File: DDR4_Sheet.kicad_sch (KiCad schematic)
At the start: 9 parts, among them U17002 Samsung K4A4G165WE-BCRC

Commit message: move DDR power decoupling capacitors into DDR4 Sheet
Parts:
- added C? (x6): 100nF X5R 10V, Capacitor_SMD:C_0402_1005Metric, symbol Device:C
- added C? (x10): 100nF X5R 6.3V, Capacitor_SMD:C_0201_0603Metric, symbol Device:C
- added C?: 1nF X5R 50V, Capacitor_SMD:C_0402_1005Metric, symbol Device:C
- added C?: 4.7uF X5R 10V, Capacitor_SMD:C_0402_1005Metric, symbol Device:C
- added C?: 22uF X5R 6.3V, Capacitor_SMD:C_0603_1608Metric, symbol Device:C
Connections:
- net V_{DD} is gone; now on net VCC1V2_DDR: U17002.B3 (V_{DD}), U17002.B9 (V_{DD}), U17002.D1 (V_{DD}), U17002.G7 (V_{DD}), U17002.J1 (V_{DD}), U17002.J9 (V_{DD}), U17002.L1 (V_{DD}), U17002.L9 (V_{DD}), U17002.R1 (V_{DD}), U17002.T9 (V_{DD})
- net V_{DDQ} renamed VCC1V2_DDR
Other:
- moved on the sheet: C?, R17002, R?, U17002B, U?A

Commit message: changed Power Label and copy DDR4 Sheets
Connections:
- net VCC1V2_DDR renamed VCC1V2

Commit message: connect new decoupling capacitors
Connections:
- net GND: now also C?.1, C?.1, C?.1, C?.1, C?.1, C?.1, C?.1, C?.1, C?.1, C?.1, C?.1, C?.1, C?.1, C?.1, C?.1, C?.1, C?.1, C?.1, C?.2
- net VCC1V2: now also C?.2, C?.2, C?.2, C?.2, C?.2, C?.2, C?.2, C?.2, C?.2, C?.2, C?.2, C?.2, C?.2, C?.2, C?.2
- net VCC2V5: now also C?.1, C?.2, C?.2, C?.2

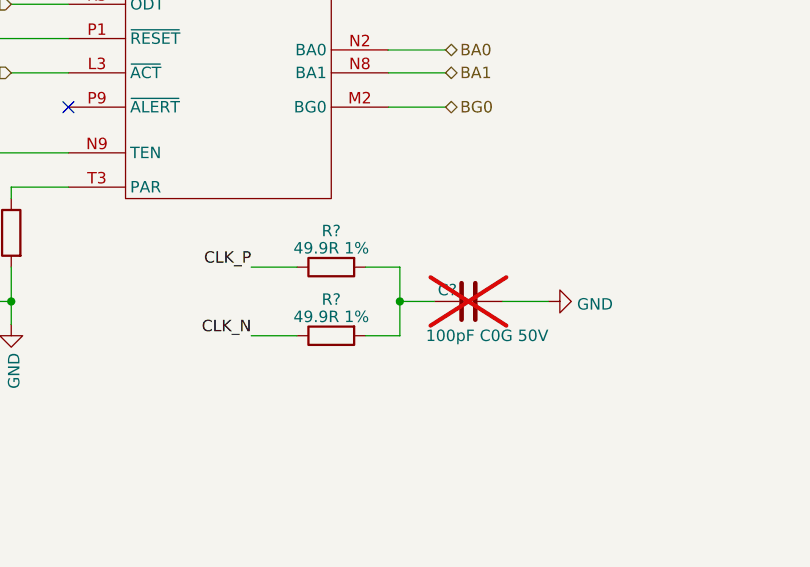
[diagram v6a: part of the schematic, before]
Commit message: remove DRC errors
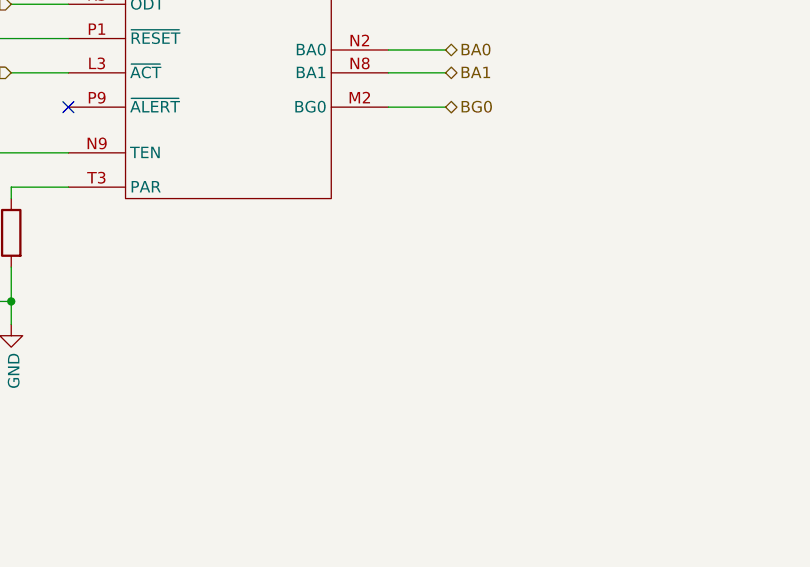
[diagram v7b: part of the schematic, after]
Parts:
- removed C?: 100pF C0G 50V, Capacitor_SMD:C_0201_0603Metric, symbol Device:C
- removed R? (x2): 49.9R 1%, Resistor_SMD:R_0402_1005Metric, symbol Device:R
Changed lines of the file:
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@@
   (junction (at 214.63 133.35) (diameter 0) (color 0 0 0 0)
-  )
-  (junction (at 114.3 119.38) (diameter 0) (color 0 0 0 0)
   )
   (junction (at 194.31 63.5) (diameter 0) (color 0 0 0 0)
@@
     (stroke (width 0) (type default))
   )
-  (wire (pts (xy 110.49 115.57) (xy 114.3 115.57))
-    (stroke (width 0) (type default))
-  )
   (wire (pts (xy 113.03 49.53) (xy 119.38 49.53))
     (stroke (width 0) (type default))
@@
     (stroke (width 0) (type default))
   )
-  (wire (pts (xy 114.3 123.19) (xy 114.3 119.38))
-    (stroke (width 0) (type default))
-  )
   (wire (pts (xy 248.92 68.58) (xy 248.92 71.12))
     (stroke (width 0) (type default))
@@
     (stroke (width 0) (type default))
   )
-  (wire (pts (xy 125.73 119.38) (xy 130.81 119.38))
-    (stroke (width 0) (type default))
-  )
   (wire (pts (xy 243.84 39.37) (xy 248.92 39.37))
     (stroke (width 0) (type default))
@@
     (stroke (width 0) (type default))
   )
-  (wire (pts (xy 97.79 123.19) (xy 102.87 123.19))
-    (stroke (width 0) (type default))
-  )
   (wire (pts (xy 77.47 62.23) (xy 71.12 62.23))
     (stroke (width 0) (type default))
@@
     (stroke (width 0) (type default))
   )
-  (wire (pts (xy 114.3 119.38) (xy 118.11 119.38))
-    (stroke (width 0) (type default))
-  )
   (wire (pts (xy 77.47 59.69) (xy 71.12 59.69))
     (stroke (width 0) (type default))
@@
     (stroke (width 0) (type default))
   )
-  (wire (pts (xy 97.79 115.57) (xy 102.87 115.57))
-    (stroke (width 0) (type default))
-  )
   (wire (pts (xy 243.84 46.99) (xy 248.92 46.99))
     (stroke (width 0) (type default))
@@
     (stroke (width 0) (type default))
   )
-  (wire (pts (xy 114.3 115.57) (xy 114.3 119.38))
-    (stroke (width 0) (type default))
-  )
   (wire (pts (xy 113.03 39.37) (xy 119.38 39.37))
     (stroke (width 0) (type default))
@@
   )
   (wire (pts (xy 184.15 129.54) (xy 184.15 133.35))
-    (stroke (width 0) (type default))
-  )
-  (wire (pts (xy 110.49 123.19) (xy 114.3 123.19))
     (stroke (width 0) (type default))
   )
@@
     (effects (font (size 1.27 1.27)) (justify left bottom))
   )
-  (label "CLK_N" (at 97.79 123.19 180) (fields_autoplaced)
-    (effects (font (size 1.27 1.27)) (justify right bottom))
-  )
   (label "VCC2V5" (at 184.15 129.54 180) (fields_autoplaced)
     (effects (font (size 1.27 1.27)) (justify right bottom))
@@
   (label "VCC2V5" (at 36.83 29.21 0) (fields_autoplaced)
     (effects (font (size 1.27 1.27)) (justify left bottom))
-  )
-  (label "CLK_P" (at 97.79 115.57 180) (fields_autoplaced)
-    (effects (font (size 1.27 1.27)) (justify right bottom))
   )
   (label "VCC1V2" (at 156.21 27.94 180) (fields_autoplaced)
@@
     )
   )
-  (symbol (lib_id "Device:R") (at 106.68 115.57 90) (mirror x) (unit 1)
-    (in_bom yes) (on_board yes) (dnp no) (fields_autoplaced)
-    (property "Reference" "R?" (at 106.68 111.5441 90)
-      (effects (font (size 1.27 1.27)))
-    )
-    (property "Value" "49.9R 1%" (at 106.68 113.4651 90)
-      (effects (font (size 1.27 1.27)))
-    )
-    (property "Footprint" "Resistor_SMD:R_0402_1005Metric" (at 106.68 113.792 90)
-      (effects (font (size 1.27 1.27)) hide)
-    )
-    (property "Datasheet" "~" (at 106.68 115.57 0)
-      (effects (font (size 1.27 1.27)) hide)
-    )
-    (pin "1")
-    (pin "2")
-    (instances
-      (project "leaf"
-        (path "/e3b58043-16a3-43c8-9fad-9c9784eebfa4/9453ad46-b3ff-4d4e-8aa6-7cc75aa0f522/f6658df5-193a-49b6-ab60-4ac3c0bbbc45"
-          (reference "R?") (unit 1)
-        )
-        (path "/e3b58043-16a3-43c8-9fad-9c9784eebfa4/9453ad46-b3ff-4d4e-8aa6-7cc75aa0f522"
-          (reference "R?") (unit 1)
-        )
-        (path "/e3b58043-16a3-43c8-9fad-9c9784eebfa4/9453ad46-b3ff-4d4e-8aa6-7cc75aa0f522/43b336b1-9a2a-4a37-8b6d-a408b4dd9ca2"
-          (reference "R24003") (unit 1)
-        )
-        (path "/e3b58043-16a3-43c8-9fad-9c9784eebfa4/9453ad46-b3ff-4d4e-8aa6-7cc75aa0f522/43b336b1-9a2a-4a37-8b6d-a408b4dd9ca2/c5996722-c916-43bd-91c1-647d75e652e6"
-          (reference "R67") (unit 1)
-        )
-        (path "/e3b58043-16a3-43c8-9fad-9c9784eebfa4/9453ad46-b3ff-4d4e-8aa6-7cc75aa0f522/43b336b1-9a2a-4a37-8b6d-a408b4dd9ca2/ee9868e4-059c-464c-a9c7-f65e4eca754e"
-          (reference "R57") (unit 1)
-        )
-      )
-    )
-  )
   (symbol (lib_id "Device:C") (at 127 181.61 180) (unit 1)
     (in_bom yes) (on_board yes) (dnp no)
@@
         (path "/e3b58043-16a3-43c8-9fad-9c9784eebfa4/9453ad46-b3ff-4d4e-8aa6-7cc75aa0f522/43b336b1-9a2a-4a37-8b6d-a408b4dd9ca2/ee9868e4-059c-464c-a9c7-f65e4eca754e"
           (reference "C125") (unit 1)
-        )
-      )
-    )
-  )
-  (symbol (lib_id "power:GND") (at 130.81 119.38 90) (mirror x) (unit 1)
-    (in_bom yes) (on_board yes) (dnp no) (fields_autoplaced)
-    (property "Reference" "#PWR?" (at 137.16 119.38 0)
-      (effects (font (size 1.27 1.27)) hide)
-    )
-    (property "Value" "GND" (at 133.985 119.6968 90)
-      (effects (font (size 1.27 1.27)) (justify right))
-    )
-    (property "Footprint" "" (at 130.81 119.38 0)
-      (effects (font (size 1.27 1.27)) hide)
-    )
-    (property "Datasheet" "" (at 130.81 119.38 0)
-      (effects (font (size 1.27 1.27)) hide)
-    )
-    (pin "1")
-    (instances
-      (project "leaf"
-        (path "/e3b58043-16a3-43c8-9fad-9c9784eebfa4/9453ad46-b3ff-4d4e-8aa6-7cc75aa0f522"
-          (reference "#PWR?") (unit 1)
-        )
-        (path "/e3b58043-16a3-43c8-9fad-9c9784eebfa4/9453ad46-b3ff-4d4e-8aa6-7cc75aa0f522/43b336b1-9a2a-4a37-8b6d-a408b4dd9ca2"
-          (reference "#PWR024003") (unit 1)
-        )
-        (path "/e3b58043-16a3-43c8-9fad-9c9784eebfa4/9453ad46-b3ff-4d4e-8aa6-7cc75aa0f522/43b336b1-9a2a-4a37-8b6d-a408b4dd9ca2/c5996722-c916-43bd-91c1-647d75e652e6"
-          (reference "#PWR0132") (unit 1)
-        )
-        (path "/e3b58043-16a3-43c8-9fad-9c9784eebfa4/9453ad46-b3ff-4d4e-8aa6-7cc75aa0f522/43b336b1-9a2a-4a37-8b6d-a408b4dd9ca2/ee9868e4-059c-464c-a9c7-f65e4eca754e"
-          (reference "#PWR0111") (unit 1)
         )
       )
@@
     )
   )
-  (symbol (lib_id "Device:R") (at 106.68 123.19 90) (mirror x) (unit 1)
-    (in_bom yes) (on_board yes) (dnp no) (fields_autoplaced)
-    (property "Reference" "R?" (at 106.68 119.1641 90)
-      (effects (font (size 1.27 1.27)))
-    )
-    (property "Value" "49.9R 1%" (at 106.68 121.0851 90)
-      (effects (font (size 1.27 1.27)))
-    )
-    (property "Footprint" "Resistor_SMD:R_0402_1005Metric" (at 106.68 121.412 90)
-      (effects (font (size 1.27 1.27)) hide)
-    )
-    (property "Datasheet" "~" (at 106.68 123.19 0)
-      (effects (font (size 1.27 1.27)) hide)
-    )
-    (pin "1")
-    (pin "2")
-    (instances
-      (project "leaf"
-        (path "/e3b58043-16a3-43c8-9fad-9c9784eebfa4/9453ad46-b3ff-4d4e-8aa6-7cc75aa0f522/f6658df5-193a-49b6-ab60-4ac3c0bbbc45"
-          (reference "R?") (unit 1)
-        )
-        (path "/e3b58043-16a3-43c8-9fad-9c9784eebfa4/9453ad46-b3ff-4d4e-8aa6-7cc75aa0f522"
-          (reference "R?") (unit 1)
-        )
-        (path "/e3b58043-16a3-43c8-9fad-9c9784eebfa4/9453ad46-b3ff-4d4e-8aa6-7cc75aa0f522/43b336b1-9a2a-4a37-8b6d-a408b4dd9ca2"
-          (reference "R24004") (unit 1)
-        )
-        (path "/e3b58043-16a3-43c8-9fad-9c9784eebfa4/9453ad46-b3ff-4d4e-8aa6-7cc75aa0f522/43b336b1-9a2a-4a37-8b6d-a408b4dd9ca2/c5996722-c916-43bd-91c1-647d75e652e6"
-          (reference "R68") (unit 1)
-        )
-        (path "/e3b58043-16a3-43c8-9fad-9c9784eebfa4/9453ad46-b3ff-4d4e-8aa6-7cc75aa0f522/43b336b1-9a2a-4a37-8b6d-a408b4dd9ca2/ee9868e4-059c-464c-a9c7-f65e4eca754e"
-          (reference "R58") (unit 1)
-        )
-      )
-    )
-  )
   (symbol (lib_id "Device:C") (at 109.22 181.61 180) (unit 1)
     (in_bom yes) (on_board yes) (dnp no)
@@
         )
       )
-    )
-  )
-  (symbol (lib_id "Device:C") (at 121.92 119.38 90) (unit 1)
-    (in_bom no) (on_board yes) (dnp yes)
-    (property "Reference" "C?" (at 120.65 118.11 90)
-      (effects (font (size 1.27 1.27)) (justify left))
-    )
-    (property "Value" "100pF C0G 50V" (at 130.81 123.19 90)
-      (effects (font (size 1.27 1.27)) (justify left))
-    )
-    (property "Footprint" "Capacitor_SMD:C_0201_0603Metric" (at 125.73 118.4148 0)
-      (effects (font (size 1.27 1.27)) hide)
-    )
-    (property "Datasheet" "~" (at 121.92 119.38 0)
-      (effects (font (size 1.27 1.27)) hide)
-    )
-    (property "LCSC" "" (at 121.92 119.38 0)
-      (effects (font (size 1.27 1.27)) hide)
-    )
-    (property "Description" "" (at 121.92 119.38 0)
-      (effects (font (size 1.27 1.27)) hide)
-    )
-    (property "Vendor" "" (at 121.92 119.38 0)
-      (effects (font (size 1.27 1.27)) hide)
-    )
-    (pin "1")
-    (pin "2")
-    (instances
-      (project "leaf"
-        (path "/e3b58043-16a3-43c8-9fad-9c9784eebfa4/9453ad46-b3ff-4d4e-8aa6-7cc75aa0f522/f6658df5-193a-49b6-ab60-4ac3c0bbbc45"
-          (reference "C?") (unit 1)
-        )
-        (path "/e3b58043-16a3-43c8-9fad-9c9784eebfa4/9453ad46-b3ff-4d4e-8aa6-7cc75aa0f522"
-          (reference "C?") (unit 1)
-        )
-        (path "/e3b58043-16a3-43c8-9fad-9c9784eebfa4/9453ad46-b3ff-4d4e-8aa6-7cc75aa0f522/43b336b1-9a2a-4a37-8b6d-a408b4dd9ca2"
-          (reference "C24002") (unit 1)
-        )
-        (path "/e3b58043-16a3-43c8-9fad-9c9784eebfa4/9453ad46-b3ff-4d4e-8aa6-7cc75aa0f522/43b336b1-9a2a-4a37-8b6d-a408b4dd9ca2/c5996722-c916-43bd-91c1-647d75e652e6"
-          (reference "C148") (unit 1)
-        )
-        (path "/e3b58043-16a3-43c8-9fad-9c9784eebfa4/9453ad46-b3ff-4d4e-8aa6-7cc75aa0f522/43b336b1-9a2a-4a37-8b6d-a408b4dd9ca2/ee9868e4-059c-464c-a9c7-f65e4eca754e"
-          (reference "C109") (unit 1)
-        )
-      )

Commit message: remove all warnings
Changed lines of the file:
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@@
-    (stroke (width 0) (type default))
-  )
-  (wire (pts (xy 156.21 27.94) (xy 163.83 27.94))
     (stroke (width 0) (type default))
   )
@@
   )
   (wire (pts (xy 68.58 185.42) (xy 73.66 185.42))
-    (stroke (width 0) (type default))
-  )
-  (wire (pts (xy 156.21 31.75) (xy 163.83 31.75))
     (stroke (width 0) (type default))
   )
@@
     (effects (font (size 1.27 1.27)) (justify right bottom))
   )
-  (label "V_{DD}" (at 163.83 27.94 0) (fields_autoplaced)
-    (effects (font (size 1.27 1.27)) (justify left bottom))
-  )
   (label "VCC2V5" (at 184.15 129.54 180) (fields_autoplaced)
     (effects (font (size 1.27 1.27)) (justify right bottom))
   )
-  (label "V_{DDQ}" (at 163.83 31.75 0) (fields_autoplaced)
-    (effects (font (size 1.27 1.27)) (justify left bottom))
-  )
   (label "VCC2V5" (at 36.83 29.21 0) (fields_autoplaced)
     (effects (font (size 1.27 1.27)) (justify left bottom))
   )
-  (label "VCC1V2" (at 156.21 27.94 180) (fields_autoplaced)
-    (effects (font (size 1.27 1.27)) (justify right bottom))
-  )
   (label "VCC1V2" (at 60.96 156.21 180) (fields_autoplaced)
     (effects (font (size 1.27 1.27)) (justify right bottom))
   )
-  (label "VCC1V2" (at 156.21 31.75 180) (fields_autoplaced)
+  (label "VCC1V2" (at 185.42 55.88 180) (fields_autoplaced)
     (effects (font (size 1.27 1.27)) (justify right bottom))
   )
-  (label "V_{DDQ}" (at 185.42 55.88 180) (fields_autoplaced)
+  (label "VCC1V2" (at 185.42 29.21 180) (fields_autoplaced)
     (effects (font (size 1.27 1.27)) (justify right bottom))
   )
-  (label "V_{DD}" (at 185.42 29.21 180) (fields_autoplaced)
-    (effects (font (size 1.27 1.27)) (justify right bottom))
-  )
